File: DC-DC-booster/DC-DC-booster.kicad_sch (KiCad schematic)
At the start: 19 parts, among them U1 MAX5026, U6 LMH6658

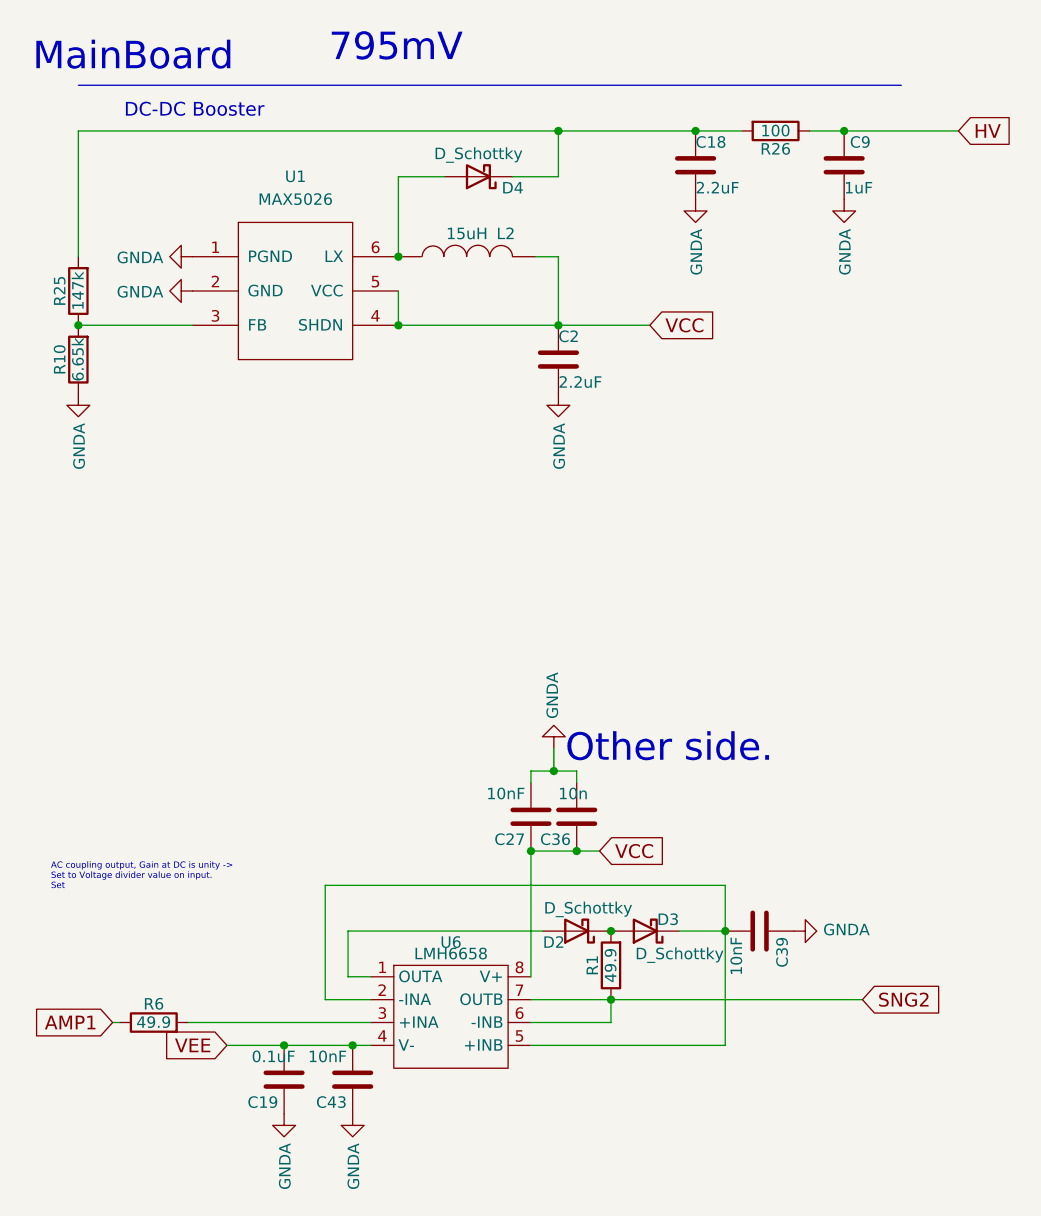
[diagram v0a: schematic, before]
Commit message: adding peak detector sketch, deleting misplaced folder
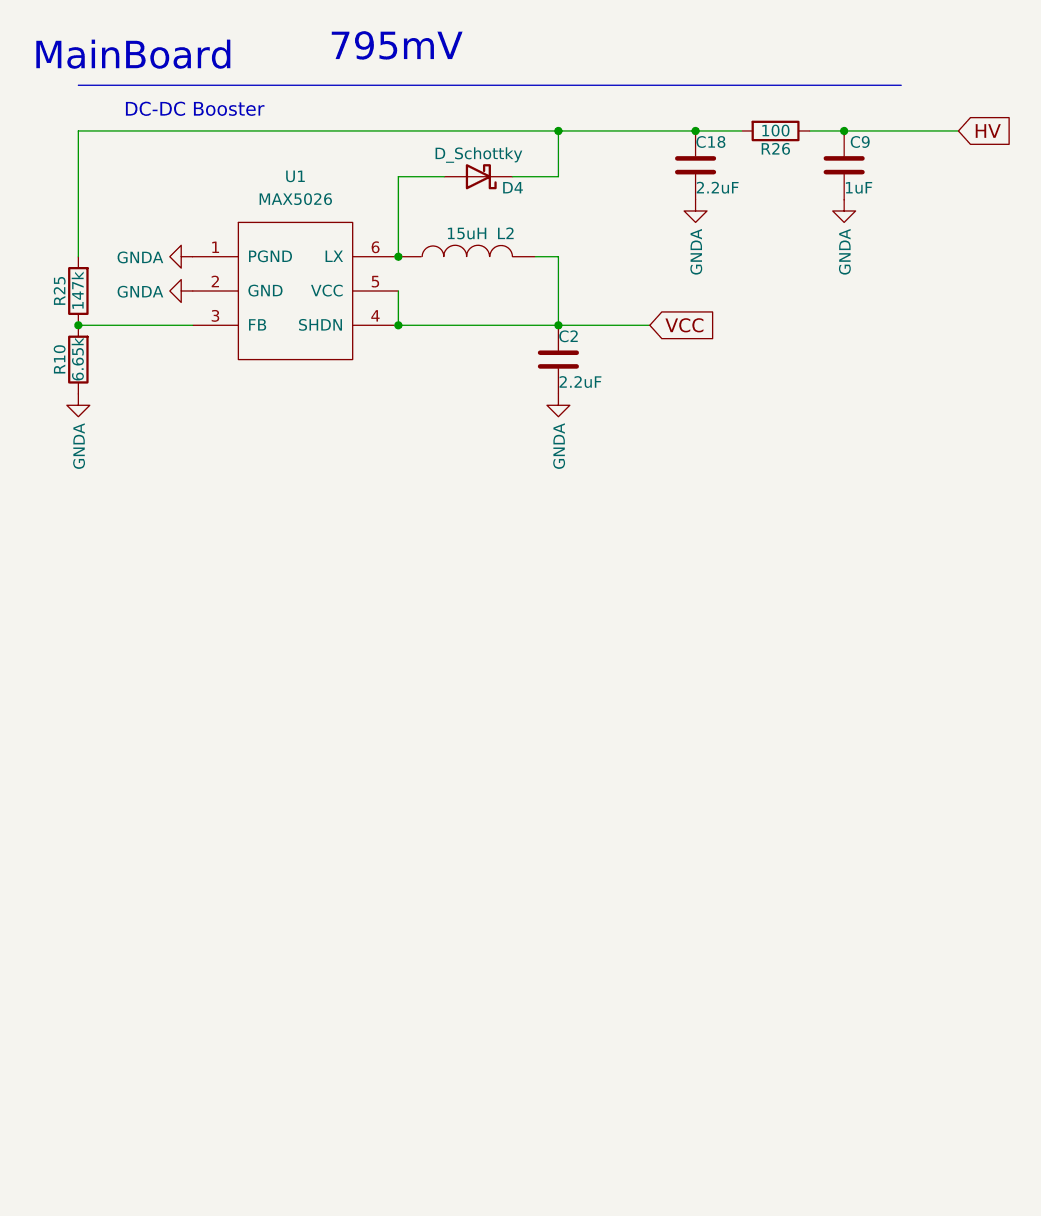
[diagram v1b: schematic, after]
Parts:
- removed C19: 0.1uF, Capacitor_SMD:C_0603_1608Metric, symbol device:C
- removed C27, C39, C43: 10nF, Capacitor_SMD:C_0603_1608Metric, symbol device:C
- removed C36: 10n, Capacitor_SMD:C_0603_1608Metric, symbol device:C
- removed D2, D3: D_Schottky, Diode_SMD:D_SOD-523, symbol My_Symbol_Library:D_Schottky
- removed R1, R6: 49.9, Capacitor_SMD:C_0603_1608Metric, symbol device:R
- removed U6: LMH6658, Package_SO:SOIC-8_3.9x4.9mm_P1.27mm, symbol My_Library:LMH6658
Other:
- note removed: "AC coupling output, Gain at DC is unity -> Set to Voltage divider value on input. Set"
- note removed: "Other side."
